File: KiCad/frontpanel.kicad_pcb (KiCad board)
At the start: 2 copper layers, 154.9 x 91.4 mm, 26 parts, among them P1 CONN_02X13, P2 CONN_02X13

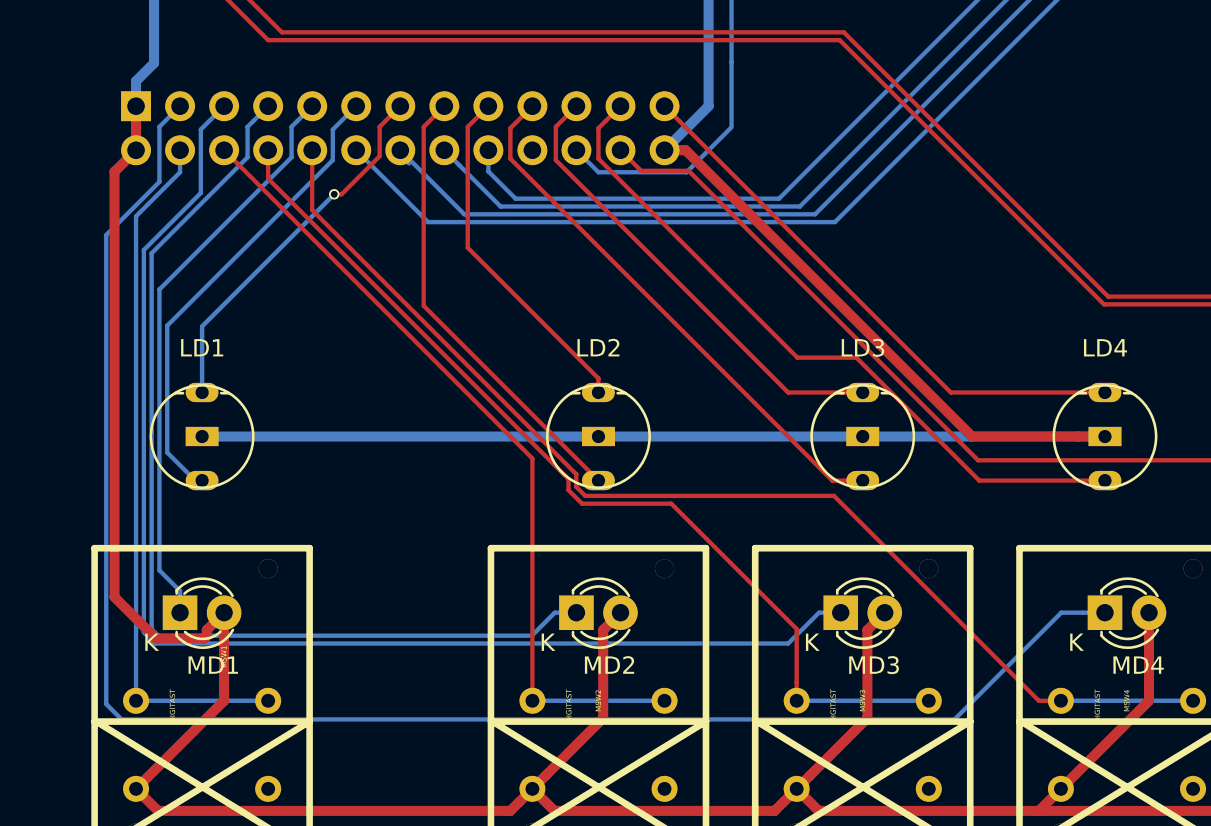
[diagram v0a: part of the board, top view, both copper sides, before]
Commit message: fixed wrong led order
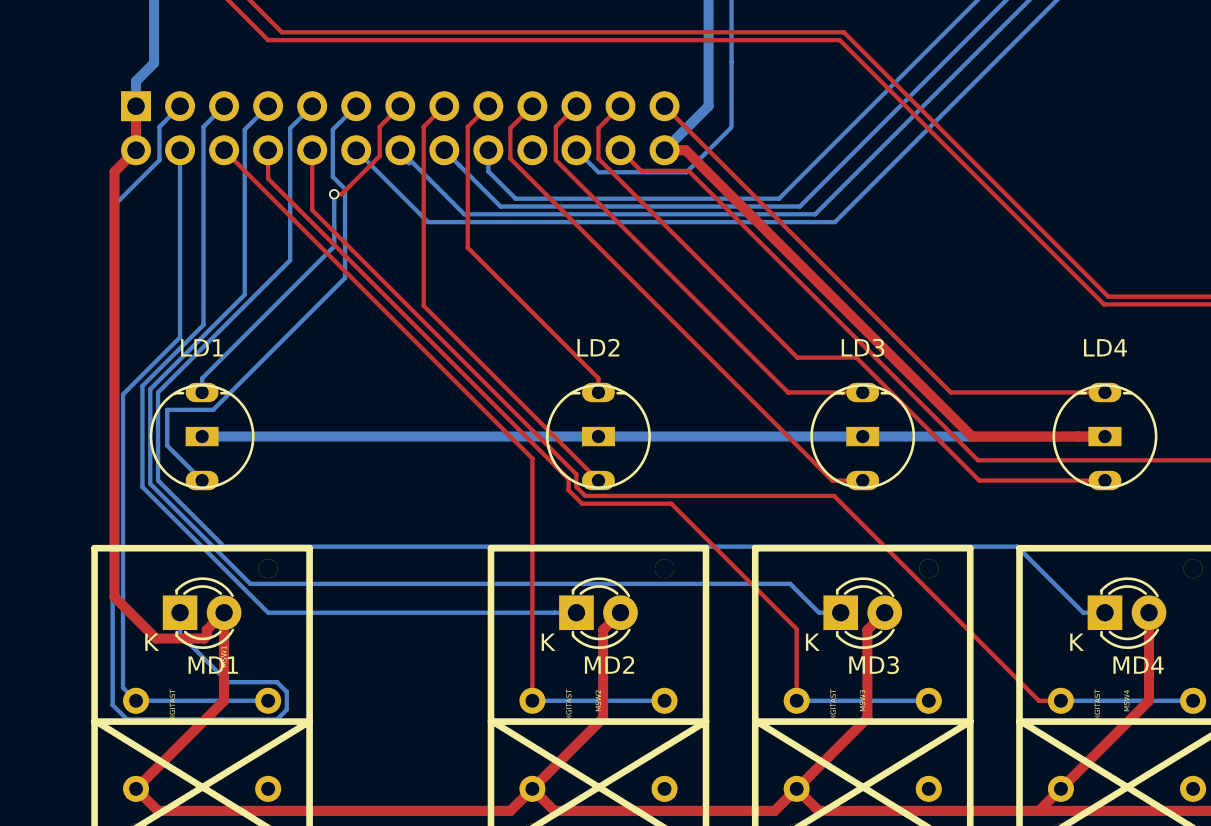
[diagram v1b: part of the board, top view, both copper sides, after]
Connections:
- P1 pad 3: Net-(MD4-Pad1) -> Net-(MD1-Pad1)
- P1 pad 5: Net-(MD3-Pad1) -> Net-(MD2-Pad1)
- P1 pad 7: Net-(MD2-Pad1) -> Net-(MD3-Pad1)
- P1 pad 9: Net-(MD1-Pad1) -> Net-(MD4-Pad1)
- RSW1 pad 0: Net-(RSW1-Pad0) -> Net-(P1-Pad20)
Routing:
- net Net-(MD1-Pad1): track 33.4 -> 56.6 mm
- net Net-(MD4-Pad1): track 96.8 -> 83.0 mm
- net Net-(RSW1-Pad0): track 7.62 -> 0.00 mm
- net Net-(P1-Pad20): track 0.00 -> 7.62 mm
- net Net-(MD2-Pad1): track 58.1 -> 51.9 mm
- net Net-(MD3-Pad1): track 73.5 -> 67.5 mm
- net Net-(LD1-Pad3): track 27.6 -> 29.5 mm
- net Net-(MSW1-Pad0): track 40.4 -> 41.0 mm

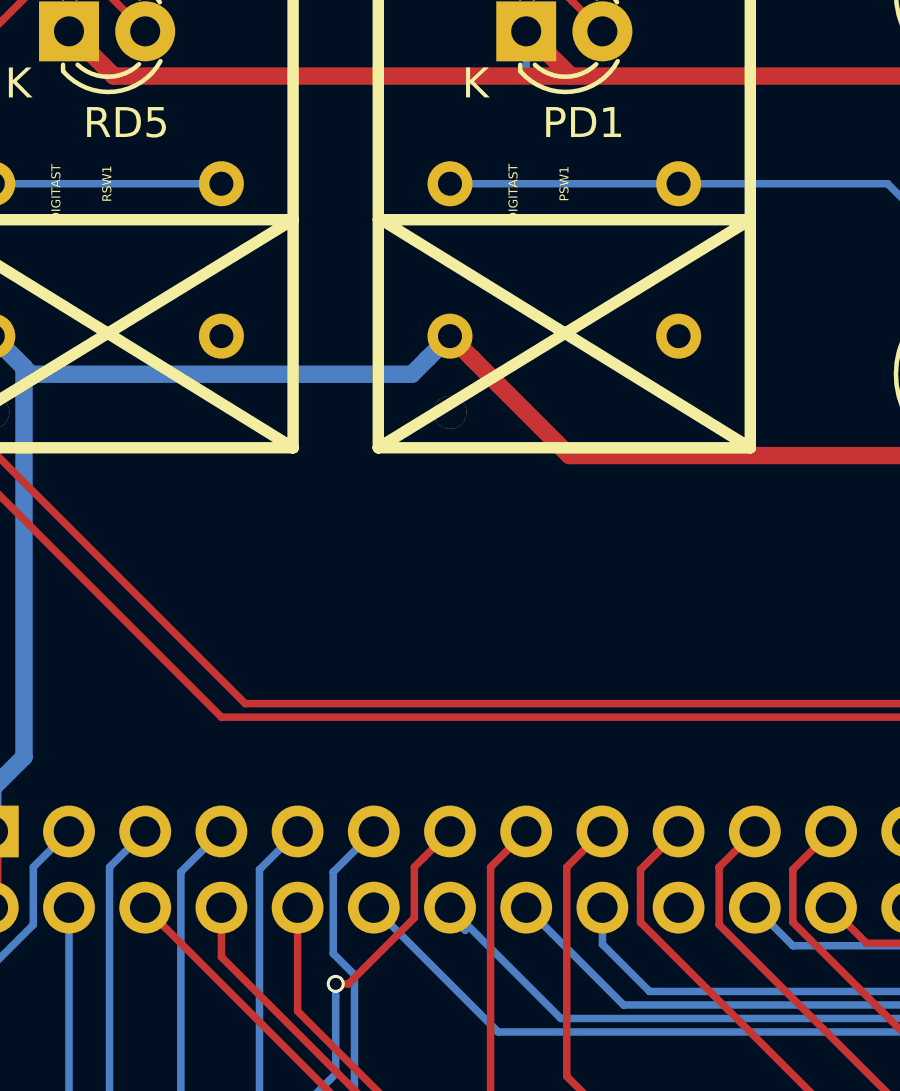
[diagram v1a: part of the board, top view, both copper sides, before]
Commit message: added missing connection
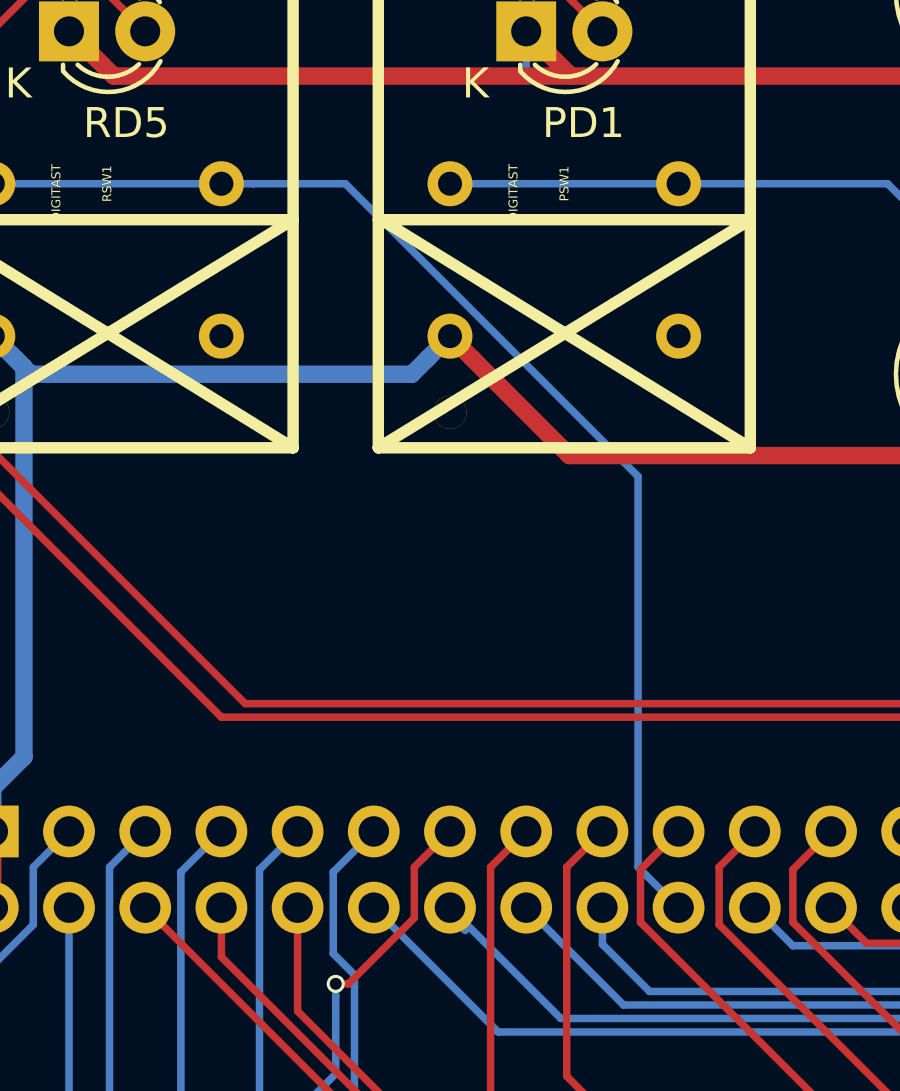
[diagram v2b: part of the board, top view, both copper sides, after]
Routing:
- net Net-(P1-Pad20): track 7.62 -> 40.5 mm
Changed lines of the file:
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@@
   (general
     (links 87)
-    (no_connects 1)
+    (no_connects 0)
     (area 68.529999 50.749999 223.570001 142.290001)
     (thickness 1.6)
     (drawings 14)
-    (tracks 435)
+    (tracks 440)
     (zones 0)
     (modules 26)
@@
   (segment (start 96.52 92.71) (end 96.52 96.161424) (width 0.25) (layer F.Cu) (net 64))
   (segment (start 111.75249 112.126086) (end 112.270214 112.64381) (width 0.25) (layer F.Cu) (net 64))
+  (segment (start 109.22 92.71) (end 107.868601 91.358601) (width 0.25) (layer B.Cu) (net 68))
+  (segment (start 107.868601 91.358601) (end 107.868601 78.336755) (width 0.25) (layer B.Cu) (net 68))
+  (segment (start 107.868601 78.336755) (end 98.111846 68.58) (width 0.25) (layer B.Cu) (net 68))
+  (segment (start 98.111846 68.58) (end 95.041466 68.58) (width 0.25) (layer B.Cu) (net 68))
+  (segment (start 95.041466 68.58) (end 93.98 68.58) (width 0.25) (layer B.Cu) (net 68))
   (segment (start 86.36 68.58) (end 93.98 68.58) (width 0.25) (layer B.Cu) (net 68))
   (segment (start 120.705001 87.63) (end 120.705001 91.384999) (width 0.25) (layer B.Cu) (net 69))
